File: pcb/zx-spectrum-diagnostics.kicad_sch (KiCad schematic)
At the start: 19 parts, among them J101 Conn_01x04, J102 Conn_01x03_Male, J103 Conn_01x03_Male, Q101 PMBT2222A, SW101 SW_SPST, SW102 SW_SPST, U101 Pico, U102 Pico

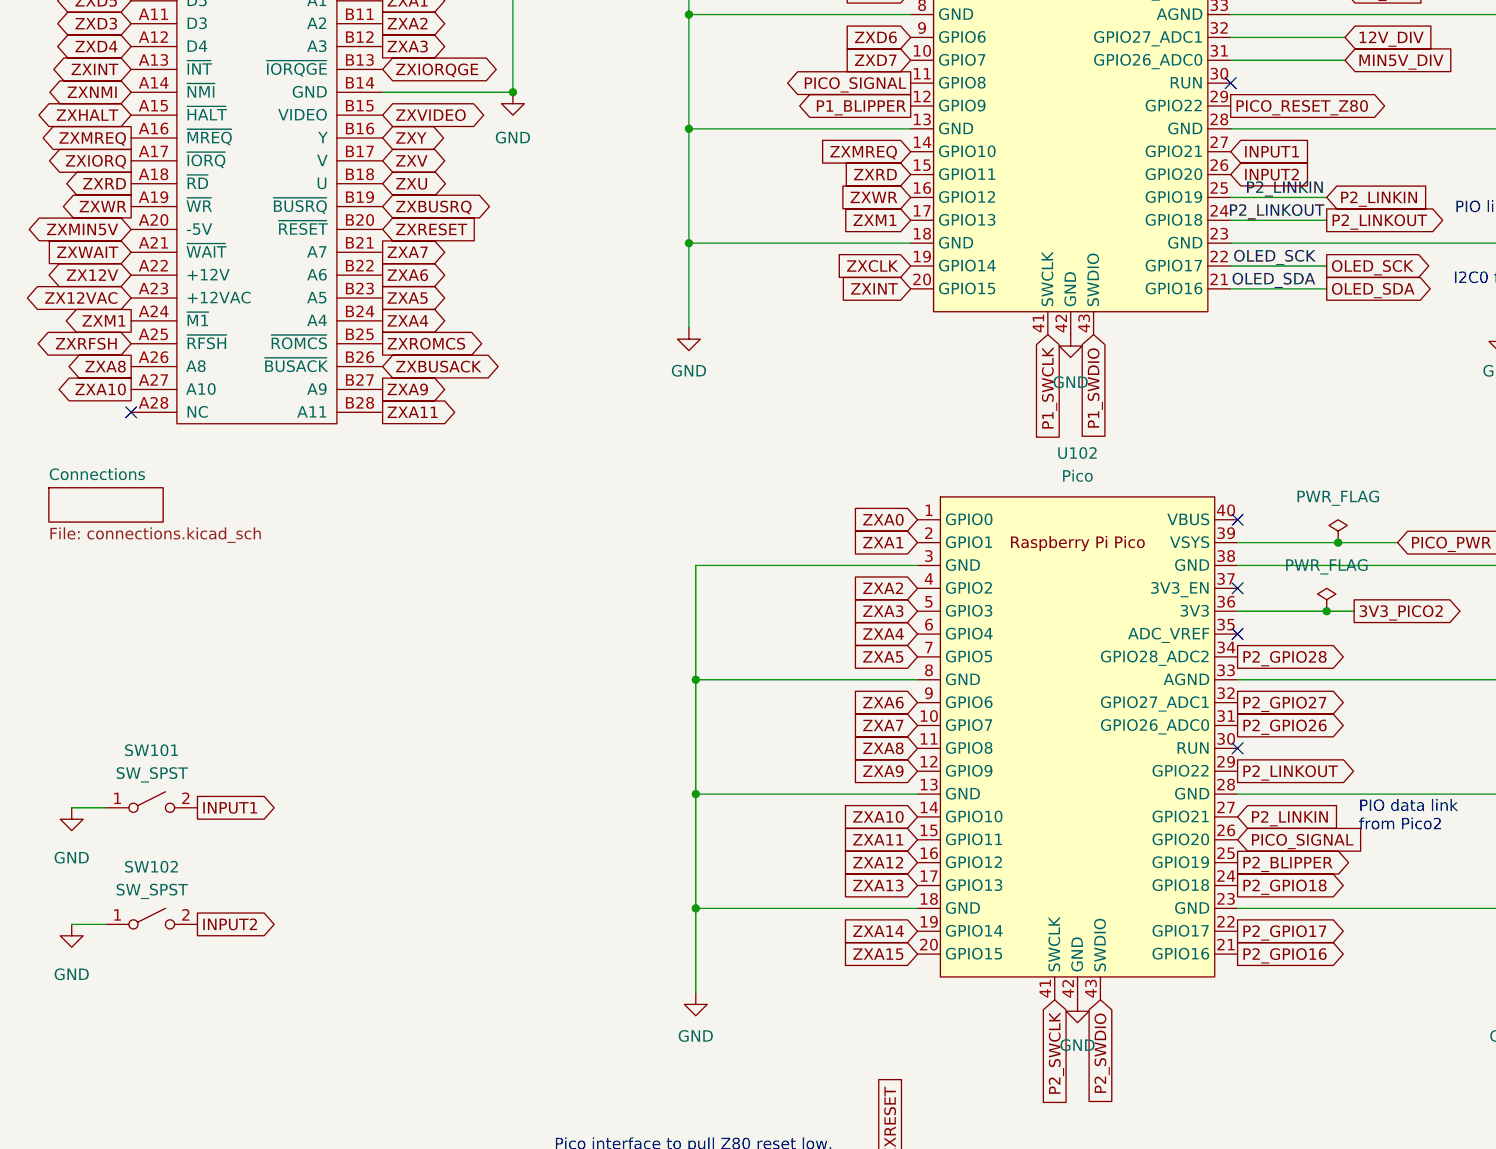
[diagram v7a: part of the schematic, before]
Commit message: remove button2, reuse GPIO for ZXIORQ
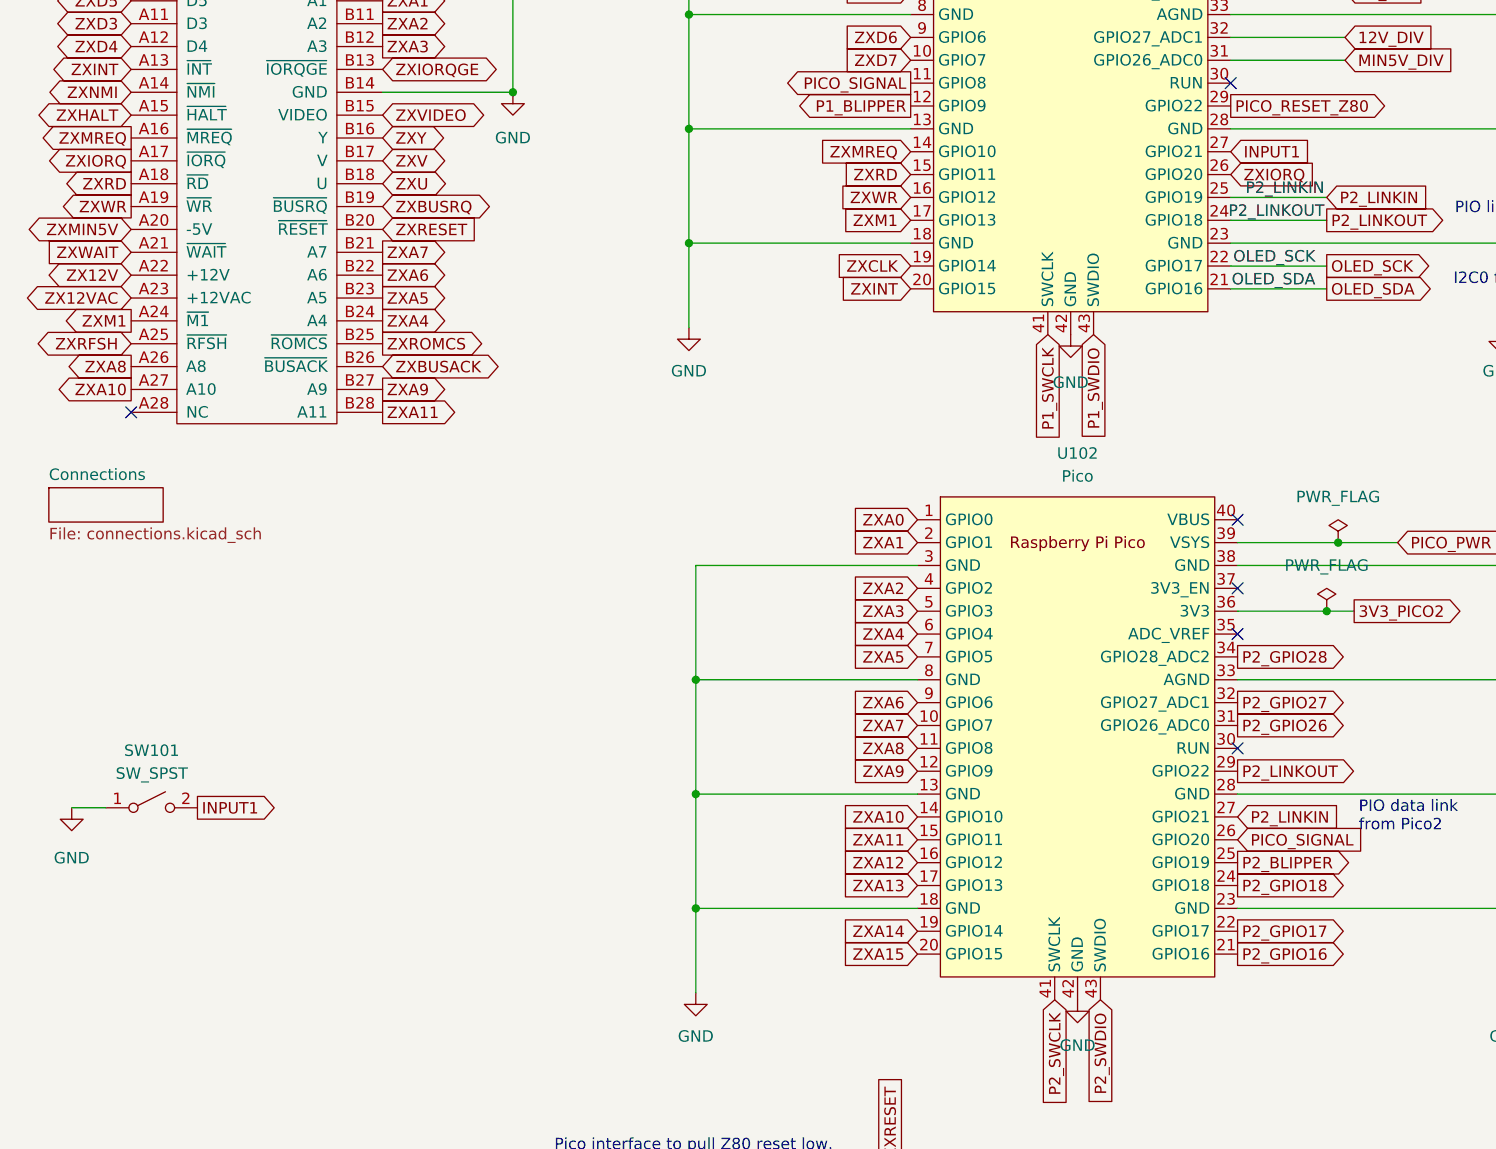
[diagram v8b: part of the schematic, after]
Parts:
- removed SW102: SW_SPST, Button_Switch_THT:SW_PUSH_6mm_H4.3mm, symbol Switch:SW_SPST
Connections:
- net INPUT2 is gone; now on net ZXIORQ: U101.26 (GPIO20)
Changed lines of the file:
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@@
-    (stroke (width 0) (type default) (color 0 0 0 0))
-  )
-  (wire (pts (xy 18.796 147.828) (xy 22.606 147.828))
     (stroke (width 0) (type default) (color 0 0 0 0))
   )
@@
     )
   )
-  (global_label "INPUT2" (shape output) (at 32.766 147.828 0) (fields_autoplaced)
-    (effects (font (size 1.27 1.27)) (justify left))
-    (property "Intersheet References" "${INTERSHEET_REFS}" (id 0) (at 41.892 147.7486 0)
-      (effects (font (size 1.27 1.27)) (justify left) hide)
-    )
-  )
   (global_label "OLED_SCK" (shape output) (at 32.766 185.674 0) (fields_autoplaced)
     (effects (font (size 1.27 1.27)) (justify left))
@@
     )
   )
-  (global_label "INPUT2" (shape input) (at 147.574 64.516 0) (fields_autoplaced)
-    (effects (font (size 1.27 1.27)) (justify left))
-    (property "Intersheet References" "${INTERSHEET_REFS}" (id 0) (at 156.7 64.4366 0)
+  (global_label "ZXIORQ" (shape input) (at 147.574 64.516 0) (fields_autoplaced)
+    (effects (font (size 1.27 1.27)) (justify left))
+    (property "Intersheet References" "${INTERSHEET_REFS}" (id 0) (at 156.9419 64.4366 0)
       (effects (font (size 1.27 1.27)) (justify left) hide)
     )
@@
     (pin "1")
   )
-  (symbol (lib_id "Switch:SW_SPST") (at 27.686 147.828 0) (unit 1)
-    (in_bom yes) (on_board yes) (fields_autoplaced)
-    (property "Reference" "SW102" (id 0) (at 27.686 141.478 0))
-    (property "Value" "SW_SPST" (id 1) (at 27.686 144.018 0))
-    (property "Footprint" "Button_Switch_THT:SW_PUSH_6mm_H4.3mm" (id 2) (at 27.686 147.828 0)
-      (effects (font (size 1.27 1.27)) hide)
-    )
-    (property "Datasheet" "~" (id 3) (at 27.686 147.828 0)
-      (effects (font (size 1.27 1.27)) hide)
-    )
-    (pin "1")
-    (pin "2")
-  )
   (symbol (lib_id "Connector_Generic:Conn_01x04") (at 25.908 185.674 180) (unit 1)
     (in_bom yes) (on_board yes) (fields_autoplaced)
@@
     (pin "1")
   )
-  (symbol (lib_id "power:GND") (at 18.796 147.828 0) (unit 1)
-    (in_bom yes) (on_board yes) (fields_autoplaced)
-    (property "Reference" "#PWR0112" (id 0) (at 18.796 154.178 0)
-      (effects (font (size 1.27 1.27)) hide)
-    )
-    (property "Value" "GND" (id 1) (at 18.796 153.416 0))
-    (property "Footprint" "" (id 2) (at 18.796 147.828 0)
-      (effects (font (size 1.27 1.27)) hide)
-    )
-    (property "Datasheet" "" (id 3) (at 18.796 147.828 0)
-      (effects (font (size 1.27 1.27)) hide)
-    )
-    (pin "1")
-  )
   (symbol (lib_id "power:GND") (at 178.308 155.702 0) (unit 1)
     (in_bom yes) (on_board yes) (fields_autoplaced)
@@
       (reference "#PWR0111") (unit 1) (value "GND") (footprint "")
     )
-    (path "/7b8fbe2f-4952-4f55-93e7-0c59f15b49f6"
-      (reference "#PWR0112") (unit 1) (value "GND") (footprint "")
-    )
     (path "/aed863a1-5b16-47c0-aa90-b3510c010e2d"
       (reference "#PWR0113") (unit 1) (value "GND") (footprint "")
@@
       (reference "SW101") (unit 1) (value "SW_SPST") (footprint "Button_Switch_THT:SW_PUSH_6mm_H4.3mm")
     )
-    (path "/3fc5c90e-db98-4999-bca2-0b14866788de"
-      (reference "SW102") (unit 1) (value "SW_SPST") (footprint "Button_Switch_THT:SW_PUSH_6mm_H4.3mm")
-    )
     (path "/5510a4fe-1794-434f-b7d2-120f1084055a"
